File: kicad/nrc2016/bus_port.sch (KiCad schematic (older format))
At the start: 3 parts

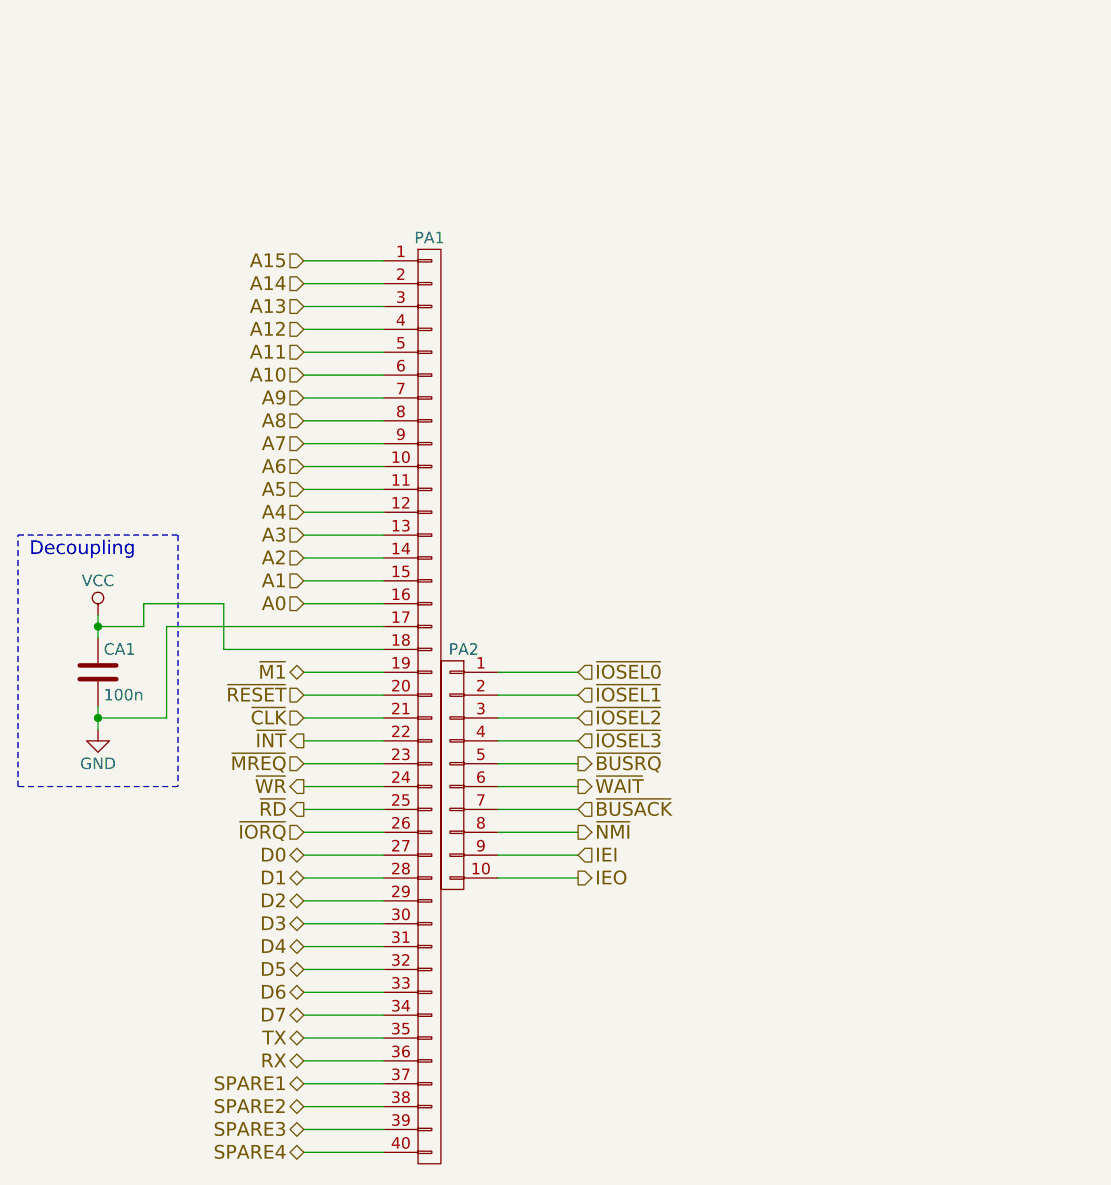
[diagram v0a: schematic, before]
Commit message: Update nrc2016 schema and PCB to use new library symbols
I've added proper schematic symbols for the pre-defined bus sockets to
stop confusion and error by just using the generic "library" socket
component and then relying on the net names to define the pins. Screwed
me once with the VCC and GND switch around, not going to happen again.
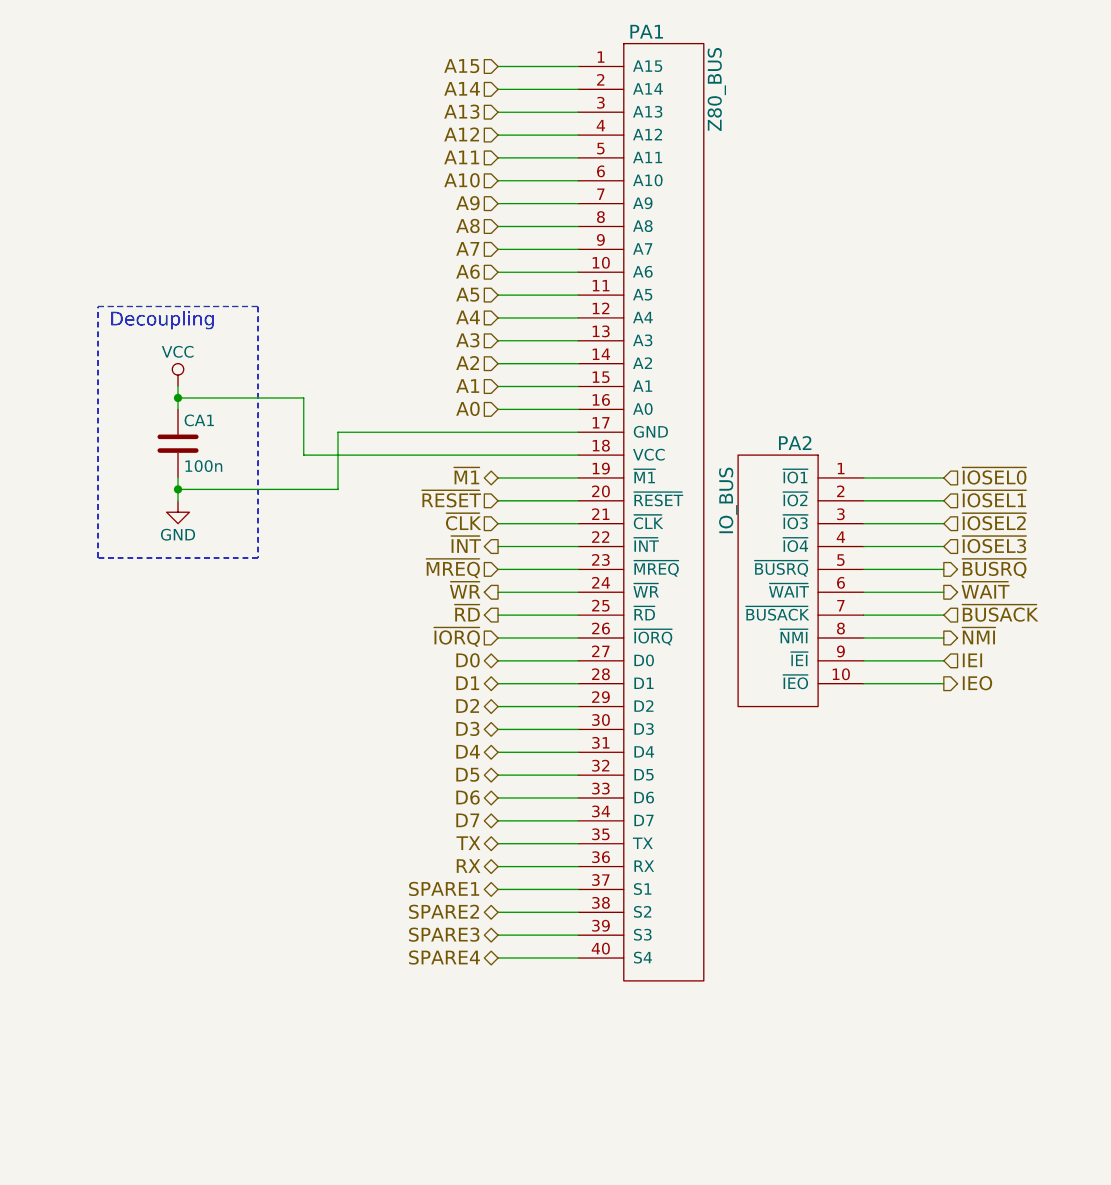
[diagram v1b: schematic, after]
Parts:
- removed PA1: CONN_01X40, Socket_Strips:Socket_Strip_Straight_1x40, symbol CONN_01X40
- removed PA2: CONN_01X10, nrc2016:Socket_Strip_Straight_1x10_NRC2016, symbol CONN_01X10
- added PA1: Z80_BUS, Socket_Strips:Socket_Strip_Straight_1x40, symbol Z80_BUS
- added PA2: IO_BUS, nrc2016:Socket_Strip_Straight_1x10_NRC2016, symbol IO_BUS
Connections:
- net A0: now also PA1.16 (A0)
- net A1: now also PA1.15 (A1)
- net A10: now also PA1.6 (A10)
- net A11: now also PA1.5 (A11)
- net A12: now also PA1.4 (A12)
- net A13: now also PA1.3 (A13)
- net A14: now also PA1.2 (A14)
- net A15: now also PA1.1 (A15)
- net A2: now also PA1.14 (A2)
- net A3: now also PA1.13 (A3)
- net A4: now also PA1.12 (A4)
- net A5: now also PA1.11 (A5)
- net A6: now also PA1.10 (A6)
- net A7: now also PA1.9 (A7)
- net A8: now also PA1.8 (A8)
- net A9: now also PA1.7 (A9)
- net D0: now also PA1.27 (D0)
- net D1: now also PA1.28 (D1)
- net D2: now also PA1.29 (D2)
- net D3: now also PA1.30 (D3)
- net D4: now also PA1.31 (D4)
- net D5: now also PA1.32 (D5)
- net D6: now also PA1.33 (D6)
- net D7: now also PA1.34 (D7)
- net GND: now also PA1.17 (GND)
- net IEI: now also PA2.9 (~IEI)
- net IEO: now also PA2.10 (~IEO)
- net RX: now also PA1.36 (RX)
- net SPARE1: now also PA1.37 (S1)
- net SPARE2: now also PA1.38 (S2)
- net SPARE3: now also PA1.39 (S3)
- net SPARE4: now also PA1.40 (S4)
- net TX: now also PA1.35 (TX)
- net VCC: now also PA1.18 (VCC)
- net ~BUSACK: now also PA2.7 (~BUSACK)
- net ~BUSRQ: now also PA2.5 (~BUSRQ)
- net ~CLK: now also PA1.21 (~CLK)
- net ~INT: now also PA1.22 (~INT)
- net ~IORQ: now also PA1.26 (~IORQ)
- net ~IOSEL0: now also PA2.1 (~IO1)
- net ~IOSEL1: now also PA2.2 (~IO2)
- net ~IOSEL2: now also PA2.3 (~IO3)
- net ~IOSEL3: now also PA2.4 (~IO4)
- net ~M1: now also PA1.19 (~M1)
- net ~MREQ: now also PA1.23 (~MREQ)
- net ~NMI: now also PA2.8 (~NMI)
- net ~RD: now also PA1.25 (~RD)
- net ~RESET: now also PA1.20 (~RESET)
- net ~WAIT: now also PA2.6 (~WAIT)
- net ~WR: now also PA1.24 (~WR)
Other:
- moved on the sheet: CA1

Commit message: More moving things around. Added sockets and pins symbols
Makes it easier for DRC and has hints for the right footprints already.
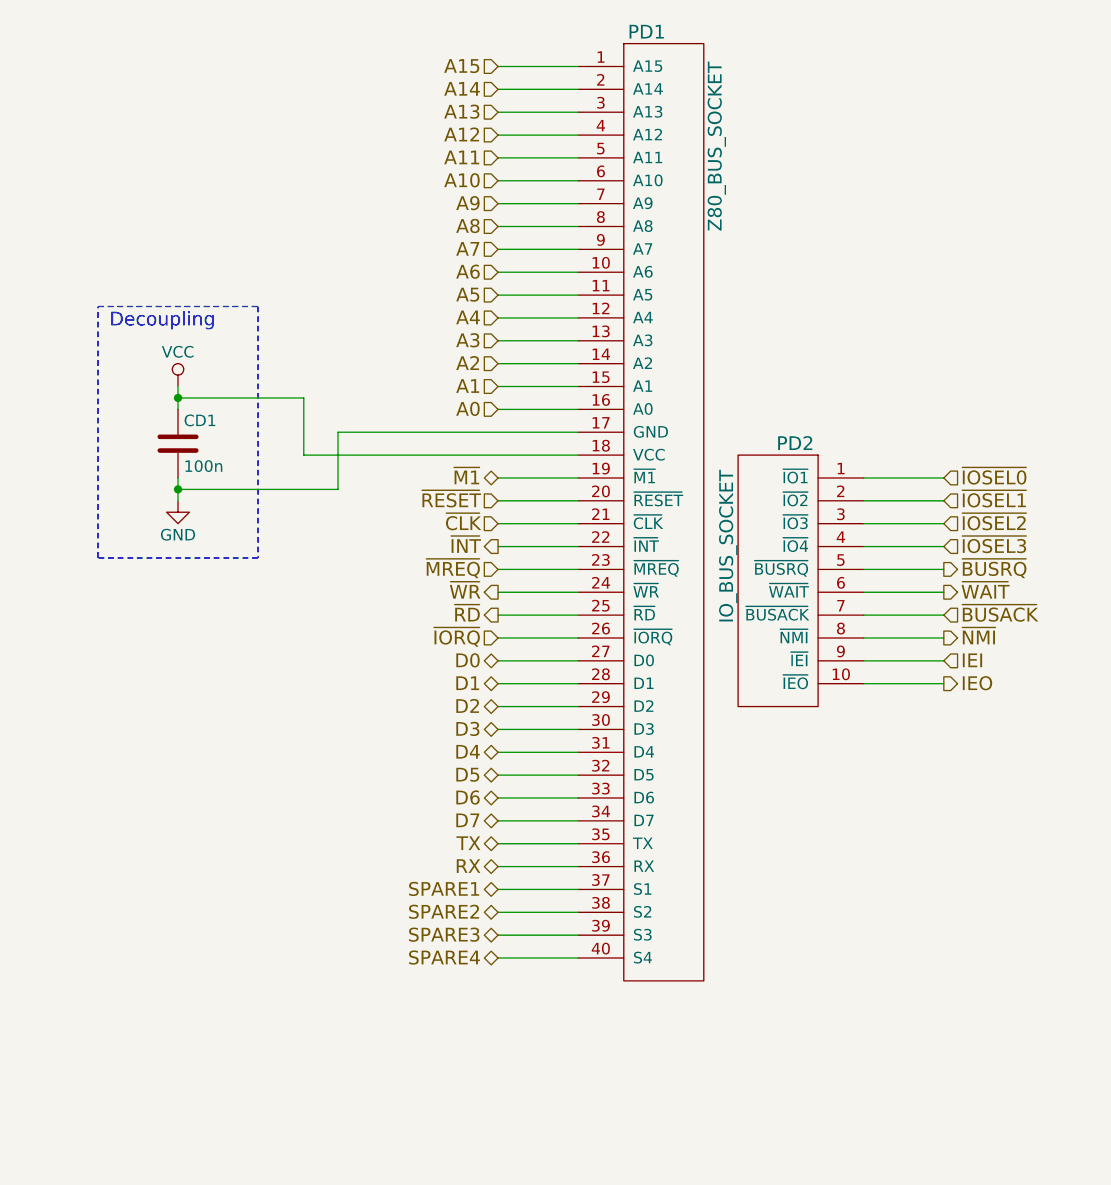
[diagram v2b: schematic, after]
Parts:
- removed PA1: Z80_BUS, Socket_Strips:Socket_Strip_Straight_1x40, symbol Z80_BUS
- removed PA2: IO_BUS, nrc2016:Socket_Strip_Straight_1x10_NRC2016, symbol IO_BUS
- added PA1: Z80_BUS_SOCKET, Socket_Strips:Socket_Strip_Straight_1x40, symbol Z80_BUS_SOCKET
- added PA2: IO_BUS_SOCKET, nrc2016:Socket_Strip_Straight_1x10_NRC2016, symbol IO_BUS_SOCKET
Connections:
- net A0: now also PA1.16 (A0)
- net A1: now also PA1.15 (A1)
- net A10: now also PA1.6 (A10)
- net A11: now also PA1.5 (A11)
- net A12: now also PA1.4 (A12)
- net A13: now also PA1.3 (A13)
- net A14: now also PA1.2 (A14)
- net A15: now also PA1.1 (A15)
- net A2: now also PA1.14 (A2)
- net A3: now also PA1.13 (A3)
- net A4: now also PA1.12 (A4)
- net A5: now also PA1.11 (A5)
- net A6: now also PA1.10 (A6)
- net A7: now also PA1.9 (A7)
- net A8: now also PA1.8 (A8)
- net A9: now also PA1.7 (A9)
- net D0: now also PA1.27 (D0)
- net D1: now also PA1.28 (D1)
- net D2: now also PA1.29 (D2)
- net D3: now also PA1.30 (D3)
- net D4: now also PA1.31 (D4)
- net D5: now also PA1.32 (D5)
- net D6: now also PA1.33 (D6)
- net D7: now also PA1.34 (D7)
- net GND: now also PA1.17 (GND)
- net IEI: now also PA2.9 (~IEI)
- net IEO: now also PA2.10 (~IEO)
- net RX: now also PA1.36 (RX)
- net SPARE1: now also PA1.37 (S1)
- net SPARE2: now also PA1.38 (S2)
- net SPARE3: now also PA1.39 (S3)
- net SPARE4: now also PA1.40 (S4)
- net TX: now also PA1.35 (TX)
- net VCC: now also PA1.18 (VCC)
- net ~BUSACK: now also PA2.7 (~BUSACK)
- net ~BUSRQ: now also PA2.5 (~BUSRQ)
- net ~CLK: now also PA1.21 (~CLK)
- net ~INT: now also PA1.22 (~INT)
- net ~IORQ: now also PA1.26 (~IORQ)
- net ~IOSEL0: now also PA2.1 (~IO1)
- net ~IOSEL1: now also PA2.2 (~IO2)
- net ~IOSEL2: now also PA2.3 (~IO3)
- net ~IOSEL3: now also PA2.4 (~IO4)
- net ~M1: now also PA1.19 (~M1)
- net ~MREQ: now also PA1.23 (~MREQ)
- net ~NMI: now also PA2.8 (~NMI)
- net ~RD: now also PA1.25 (~RD)
- net ~RESET: now also PA1.20 (~RESET)
- net ~WAIT: now also PA2.6 (~WAIT)
- net ~WR: now also PA1.24 (~WR)
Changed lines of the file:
@@
 $Descr A4 11693 8268
 encoding utf-8
-Sheet 4 8
+Sheet 7 8
 Title ""
 Date ""
@@
 AR Path="/577F17CE/5797AD5E/5780CE22" Ref="CD1"  Part="1"
 AR Path="/577F17CE/5798778E/5780CE22" Ref="CE1"  Part="1"
-F 0 "CA1" H 3375 3650 50  0000 L CNN
+F 0 "CD1" H 3375 3650 50  0000 L CNN
 F 1 "100n" H 3375 3450 50  0000 L CNN
 F 2 "Capacitors_ThroughHole:C_Rect_L4_W2.5_P2.5" H 3388 3400 50  0001 C CNN
@@
 AR Path="/577F17CE/5797AD5E/5780D6F2" Ref="#PWR031"  Part="1"
 AR Path="/577F17CE/5798778E/5780D6F2" Ref="#PWR036"  Part="1"
-F 0 "#PWR025" H 3350 3150 50  0001 C CNN
+F 0 "#PWR031" H 3350 3150 50  0001 C CNN
 F 1 "VCC" H 3350 3450 50  0000 C CNN
 F 2 "" H 3350 3300 50  0000 C CNN
@@
 AR Path="/577F17CE/5797AD5E/5780D706" Ref="#PWR032"  Part="1"
 AR Path="/577F17CE/5798778E/5780D706" Ref="#PWR037"  Part="1"
-F 0 "#PWR026" H 3350 3550 50  0001 C CNN
+F 0 "#PWR032" H 3350 3550 50  0001 C CNN
 F 1 "GND" H 3350 3650 50  0000 C CNN
 F 2 "" H 3350 3800 50  0000 C CNN
@@
 Wire Wire Line
 	3350 3700 3350 3800
-$Comp
-L Z80_BUS PA1
-U 1 1 57D43211
+Wire Wire Line
+	5100 3600 3900 3600
+Wire Wire Line
+	3900 3600 3900 3350
+Wire Wire Line
+	3900 3350 3350 3350
+Connection ~ 3350 3350
+Wire Wire Line
+	5100 3500 4050 3500
+Wire Wire Line
+	4050 3500 4050 3750
+Wire Wire Line
+	4050 3750 3350 3750
+Connection ~ 3350 3750
+$Comp
+L Z80_BUS_SOCKET PA1
+U 1 1 57D4289A
 P 5300 1800
-AR Path="/577F17CE/577F1897/57D43211" Ref="PA1"  Part="1"
-AR Path="/577F17CE/57978710/57D43211" Ref="PB1"  Part="1"
-AR Path="/577F17CE/5797AC61/57D43211" Ref="PC1"  Part="1"
-AR Path="/577F17CE/5797AD5E/57D43211" Ref="PD1"  Part="1"
-F 0 "PA1" H 5400 1850 60  0000 C CNN
-F 1 "Z80_BUS" V 5700 1600 60  0000 C CNN
+AR Path="/577F17CE/577F1897/57D4289A" Ref="PA1"  Part="1"
+AR Path="/577F17CE/57978710/57D4289A" Ref="PB1"  Part="1"
+AR Path="/577F17CE/5797AC61/57D4289A" Ref="PC1"  Part="1"
+AR Path="/577F17CE/5797AD5E/57D4289A" Ref="PD1"  Part="1"
+F 0 "PD1" H 5400 1850 60  0000 C CNN
+F 1 "Z80_BUS_SOCKET" V 5700 1350 60  0000 C CNN
 F 2 "Socket_Strips:Socket_Strip_Straight_1x40" H 5100 1900 60  0001 C CNN
 F 3 "" H 5100 1900 60  0000 C CNN
@@
 $EndComp
 $Comp
-L IO_BUS PA2
-U 1 1 57D43271
+L IO_BUS_SOCKET PA2
+U 1 1 57D427C3
 P 6150 3600
-AR Path="/577F17CE/577F1897/57D43271" Ref="PA2"  Part="1"
-AR Path="/577F17CE/57978710/57D43271" Ref="PB2"  Part="1"
-AR Path="/577F17CE/5797AC61/57D43271" Ref="PC2"  Part="1"
-AR Path="/577F17CE/5797AD5E/57D43271" Ref="PD2"  Part="1"
-F 0 "PA2" H 6250 3650 60  0000 C CNN
-F 1 "IO_BUS" V 6550 3400 60  0000 C CNN
+AR Path="/577F17CE/577F1897/57D427C3" Ref="PA2"  Part="1"
+AR Path="/577F17CE/57978710/57D427C3" Ref="PB2"  Part="1"
+AR Path="/577F17CE/5797AC61/57D427C3" Ref="PC2"  Part="1"
+AR Path="/577F17CE/5797AD5E/57D427C3" Ref="PD2"  Part="1"
+F 0 "PD2" H 6250 3650 60  0000 C CNN
+F 1 "IO_BUS_SOCKET" V 6550 3200 60  0000 C CNN
 F 2 "nrc2016:Socket_Strip_Straight_1x10_NRC2016" H 6150 3700 60  0001 C CNN
 F 3 "" H 6150 3700 60  0000 C CNN
@@
 	-1   0    0    -1
 $EndComp
-Wire Wire Line
-	5100 3600 3900 3600
-Wire Wire Line
-	3900 3600 3900 3350
-Wire Wire Line
-	3900 3350 3350 3350
-Connection ~ 3350 3350
-Wire Wire Line
-	5100 3500 4050 3500
-Wire Wire Line
-	4050 3500 4050 3750
-Wire Wire Line
-	4050 3750 3350 3750
-Connection ~ 3350 3750
 $EndSCHEMATC
